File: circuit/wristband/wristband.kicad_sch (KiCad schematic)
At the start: 81 parts, among them CN2 USBMICRO_20329, IC1 LT6230, IC2 LT6230, IC3 LT6230, IC4 LT6230, IC5 LT6230, IC6 LT6230

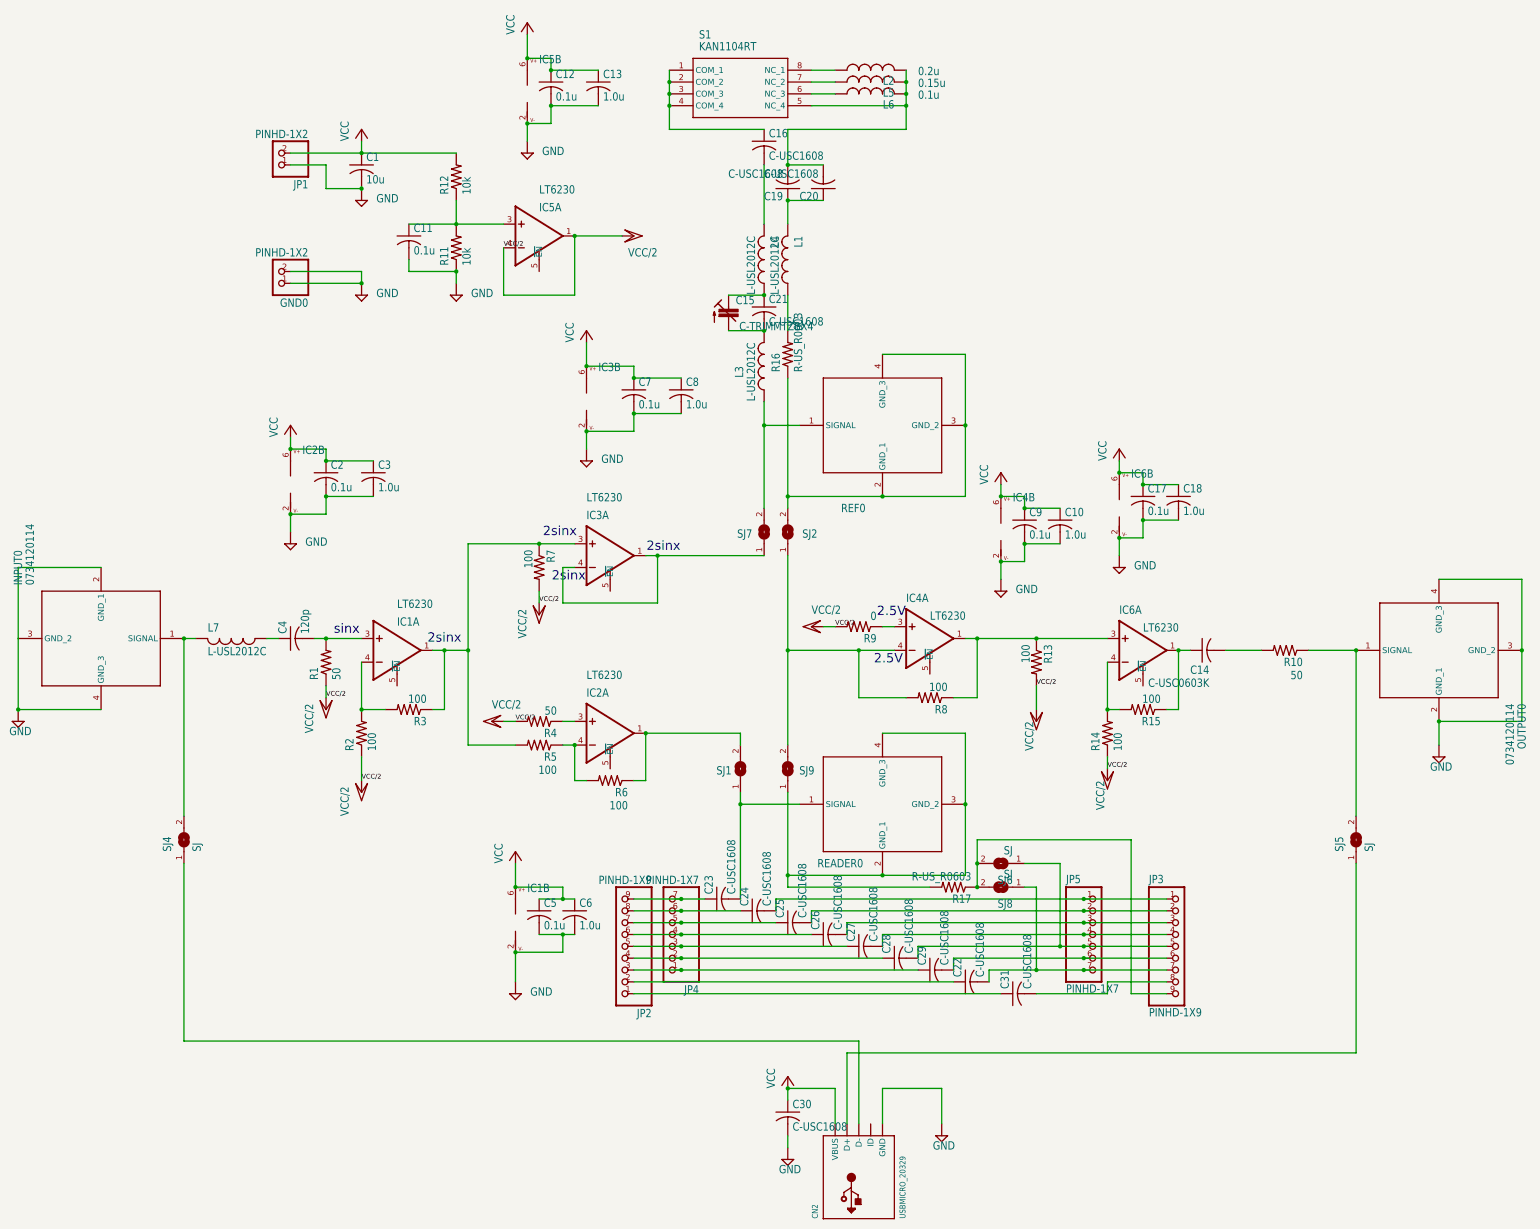
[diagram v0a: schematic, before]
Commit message: add wristband
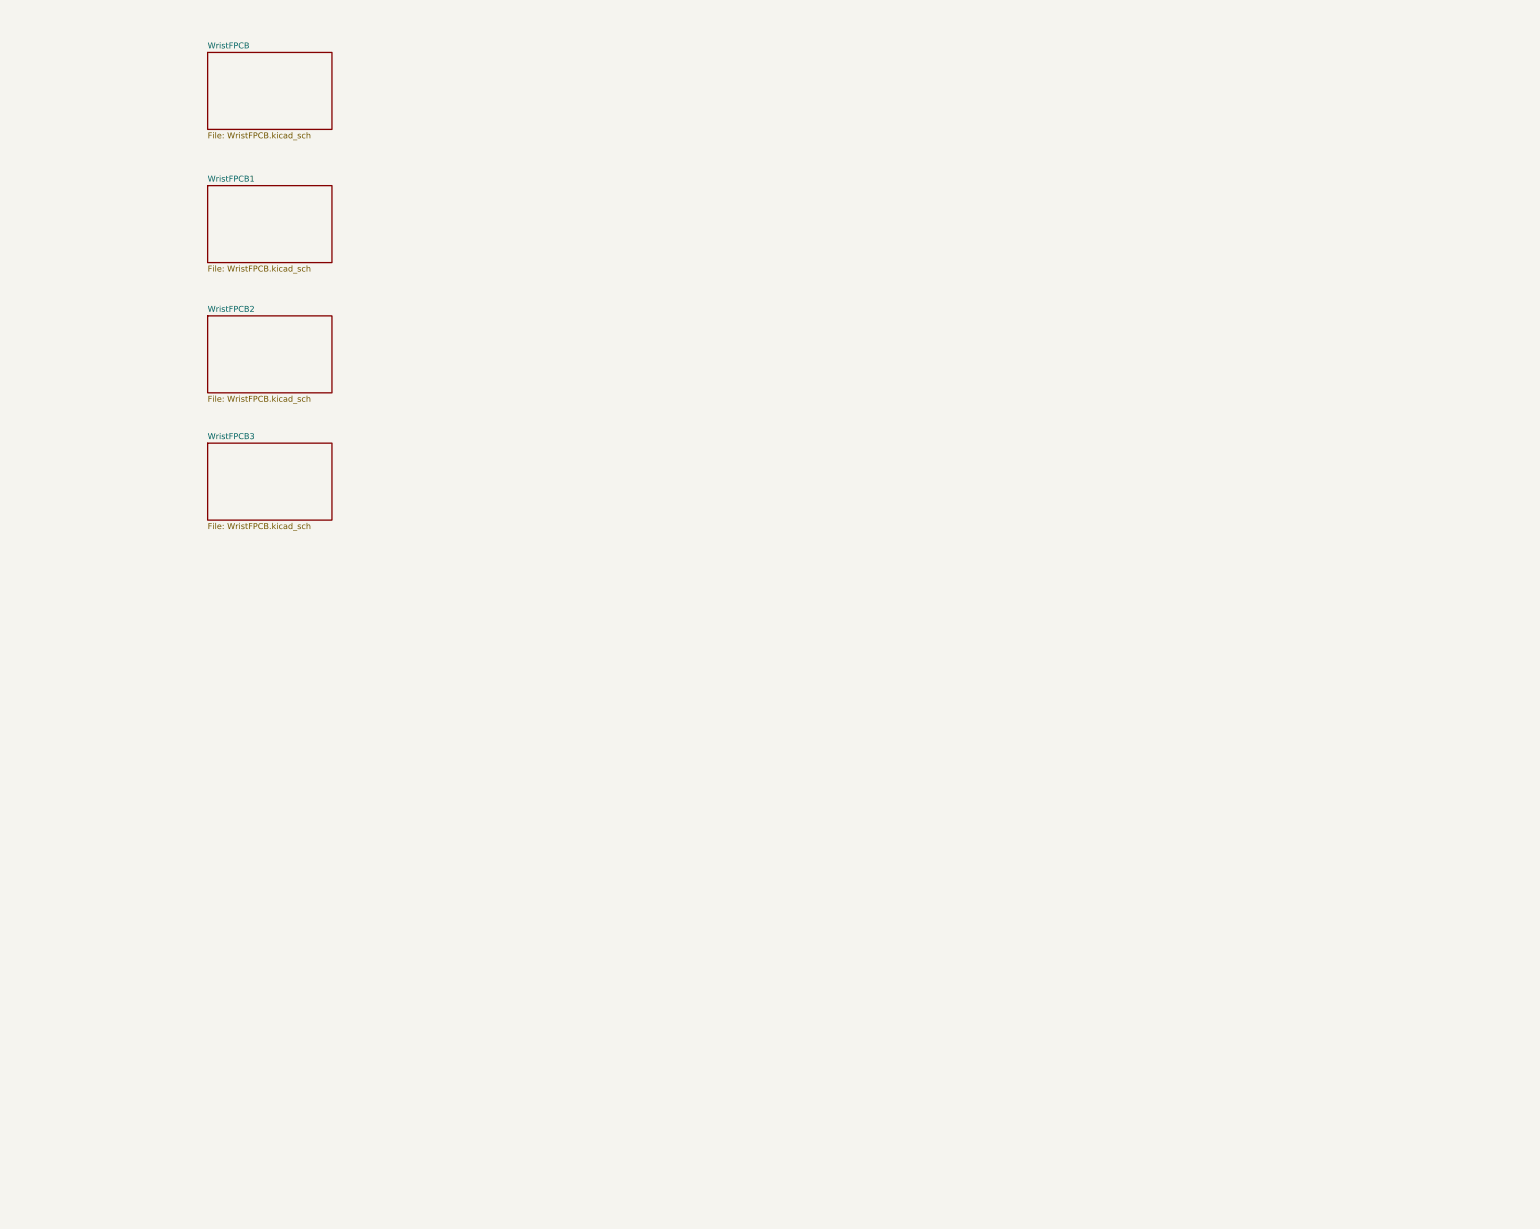
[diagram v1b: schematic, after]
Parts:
- removed C1: 10u, bridge_ver3:C0603K, symbol bridge_ver3-eagle-import:C-USC0603K
- removed C10, C13, C18, C3, C6, C8: 1.0u, bridge_ver3:C0603K, symbol bridge_ver3-eagle-import:C-USC0603K
- removed C11, C12, C17, C2, C5, C7, C9: 0.1u, bridge_ver3:C0603K, symbol bridge_ver3-eagle-import:C-USC0603K
- removed C14: C-USC0603K, bridge_ver3:C0603K, symbol bridge_ver3-eagle-import:C-USC0603K
- removed C15: C-TRIMMTZBX4, bridge_ver3:CTRIMTZBX4, symbol bridge_ver3-eagle-import:C-TRIMMTZBX4
- removed C16, C19, C20, C21, C22, C23, C24, C25, C26, C27, C28, C29, C30, C31: C-USC1608, bridge_ver3:C1608, symbol bridge_ver3-eagle-import:C-USC1608
- removed C4: 120p, bridge_ver3:C0603K, symbol bridge_ver3-eagle-import:C-USC0603K
- removed CN2: USBMICRO_20329, bridge_ver3:4UCONN_20329, symbol bridge_ver3-eagle-import:USBMICRO_20329
- removed GND0, JP1: PINHD-1X2, bridge_ver3:1X02, symbol bridge_ver3-eagle-import:PINHD-1X2
- removed IC1, IC2, IC3, IC4, IC5, IC6: LT6230, bridge_ver3:TSOT23-6, symbol bridge_ver3-eagle-import:LT6230
- removed INPUT0, OUTPUT0, READER0, REF0: 0734120114, bridge_ver3:0734120114, symbol bridge_ver3-eagle-import:0734120114
- removed JP2, JP3: PINHD-1X9, bridge_ver3:1X09, symbol bridge_ver3-eagle-import:PINHD-1X9
- removed JP4, JP5: PINHD-1X7, bridge_ver3:1X07, symbol bridge_ver3-eagle-import:PINHD-1X7
- removed L1, L3, L4, L7: L-USL2012C, bridge_ver3:L2012C, symbol bridge_ver3-eagle-import:L-USL2012C
- removed L2: 0.2u, bridge_ver3:L2012C, symbol bridge_ver3-eagle-import:L-USL2012C
- removed L5: 0.15u, bridge_ver3:L2012C, symbol bridge_ver3-eagle-import:L-USL2012C
- removed L6: 0.1u, bridge_ver3:L2012C, symbol bridge_ver3-eagle-import:L-USL2012C
- removed R1, R10, R4: 50, bridge_ver3:R0603, symbol bridge_ver3-eagle-import:R-US_R0603
- removed R11, R12: 10k, bridge_ver3:R0603, symbol bridge_ver3-eagle-import:R-US_R0603
- removed R13, R14, R15, R2, R3, R5, R6, R7, R8: 100, bridge_ver3:R0603, symbol bridge_ver3-eagle-import:R-US_R0603
- removed R16, R17: R-US_R0603, bridge_ver3:R0603, symbol bridge_ver3-eagle-import:R-US_R0603
- removed R9: 0, bridge_ver3:R0603, symbol bridge_ver3-eagle-import:R-US_R0603
- removed S1: KAN1104RT, bridge_ver3:KAN1104RT, symbol bridge_ver3-eagle-import:KAN1104RT
- removed SJ1, SJ2, SJ4, SJ5, SJ6, SJ7, SJ8, SJ9: SJ, bridge_ver3:SJ, symbol bridge_ver3-eagle-import:SJ
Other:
- added sheet WristFPCB (WristFPCB.kicad_sch)
- added sheet WristFPCB1 (WristFPCB.kicad_sch)
- added sheet WristFPCB2 (WristFPCB.kicad_sch)
- added sheet WristFPCB3 (WristFPCB.kicad_sch)
- note removed: "2.5V"
- note removed: "2sinx"
- note removed: "sinx"
